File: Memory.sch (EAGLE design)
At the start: 4 parts, among them IC5 HM62256DIP

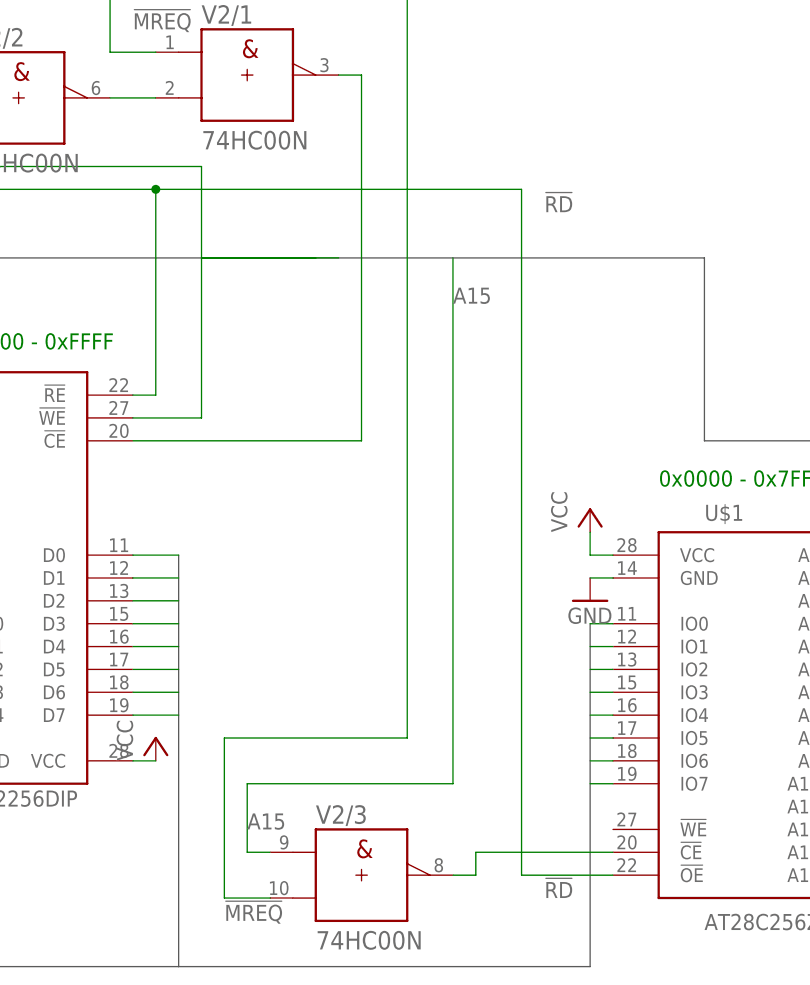
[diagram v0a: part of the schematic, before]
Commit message: Connect ROM WriteEnable so we can rewrite rom from the CPU
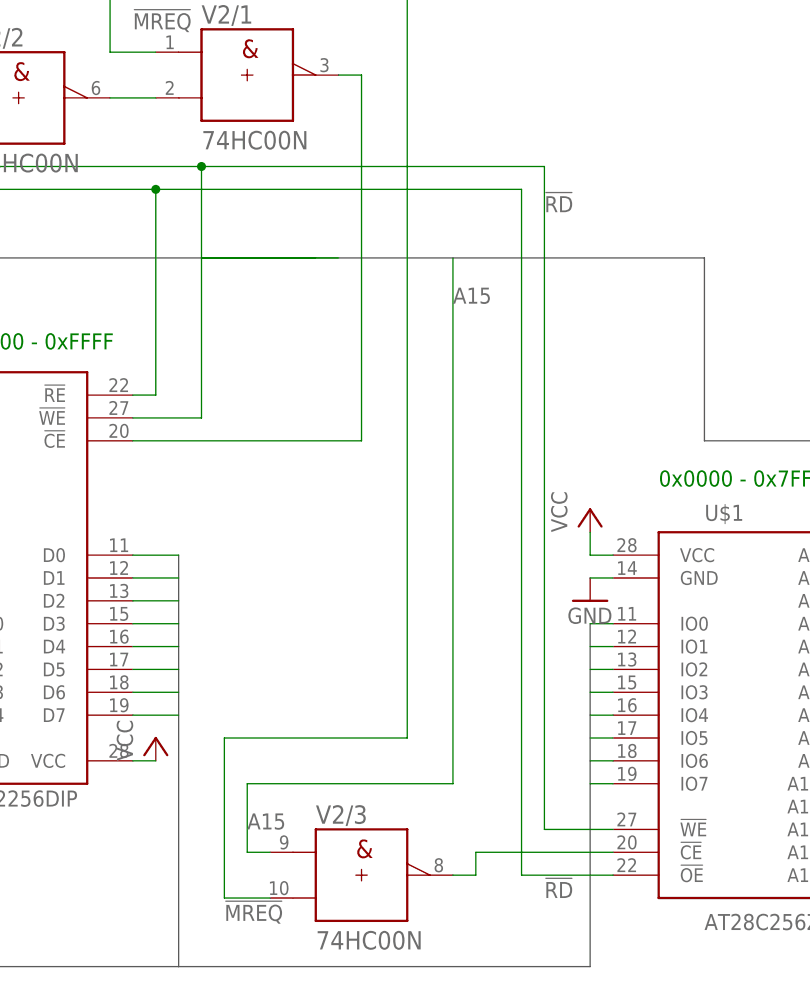
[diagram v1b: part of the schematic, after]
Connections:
- net !WR: now also U$1.!WE
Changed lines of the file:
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@@
 <wire x1="-66.04" y1="172.72" x2="-50.8" y2="172.72" width="0.1524" layer="91"/>
 <wire x1="-50.8" y1="172.72" x2="-50.8" y2="177.8" width="0.1524" layer="91"/>
+<wire x1="68.58" y1="177.8" x2="106.68" y2="177.8" width="0.1524" layer="91"/>
+<wire x1="106.68" y1="177.8" x2="106.68" y2="104.14" width="0.1524" layer="91"/>
+<junction x="68.58" y="177.8"/>
+<pinref part="U$1" gate="G$1" pin="!WE"/>
+<wire x1="106.68" y1="104.14" x2="114.3" y2="104.14" width="0.1524" layer="91"/>
 </segment>
 </net>

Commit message: Finish Modularization
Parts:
- renumbered IC5 to IC2, U$1 to IC1

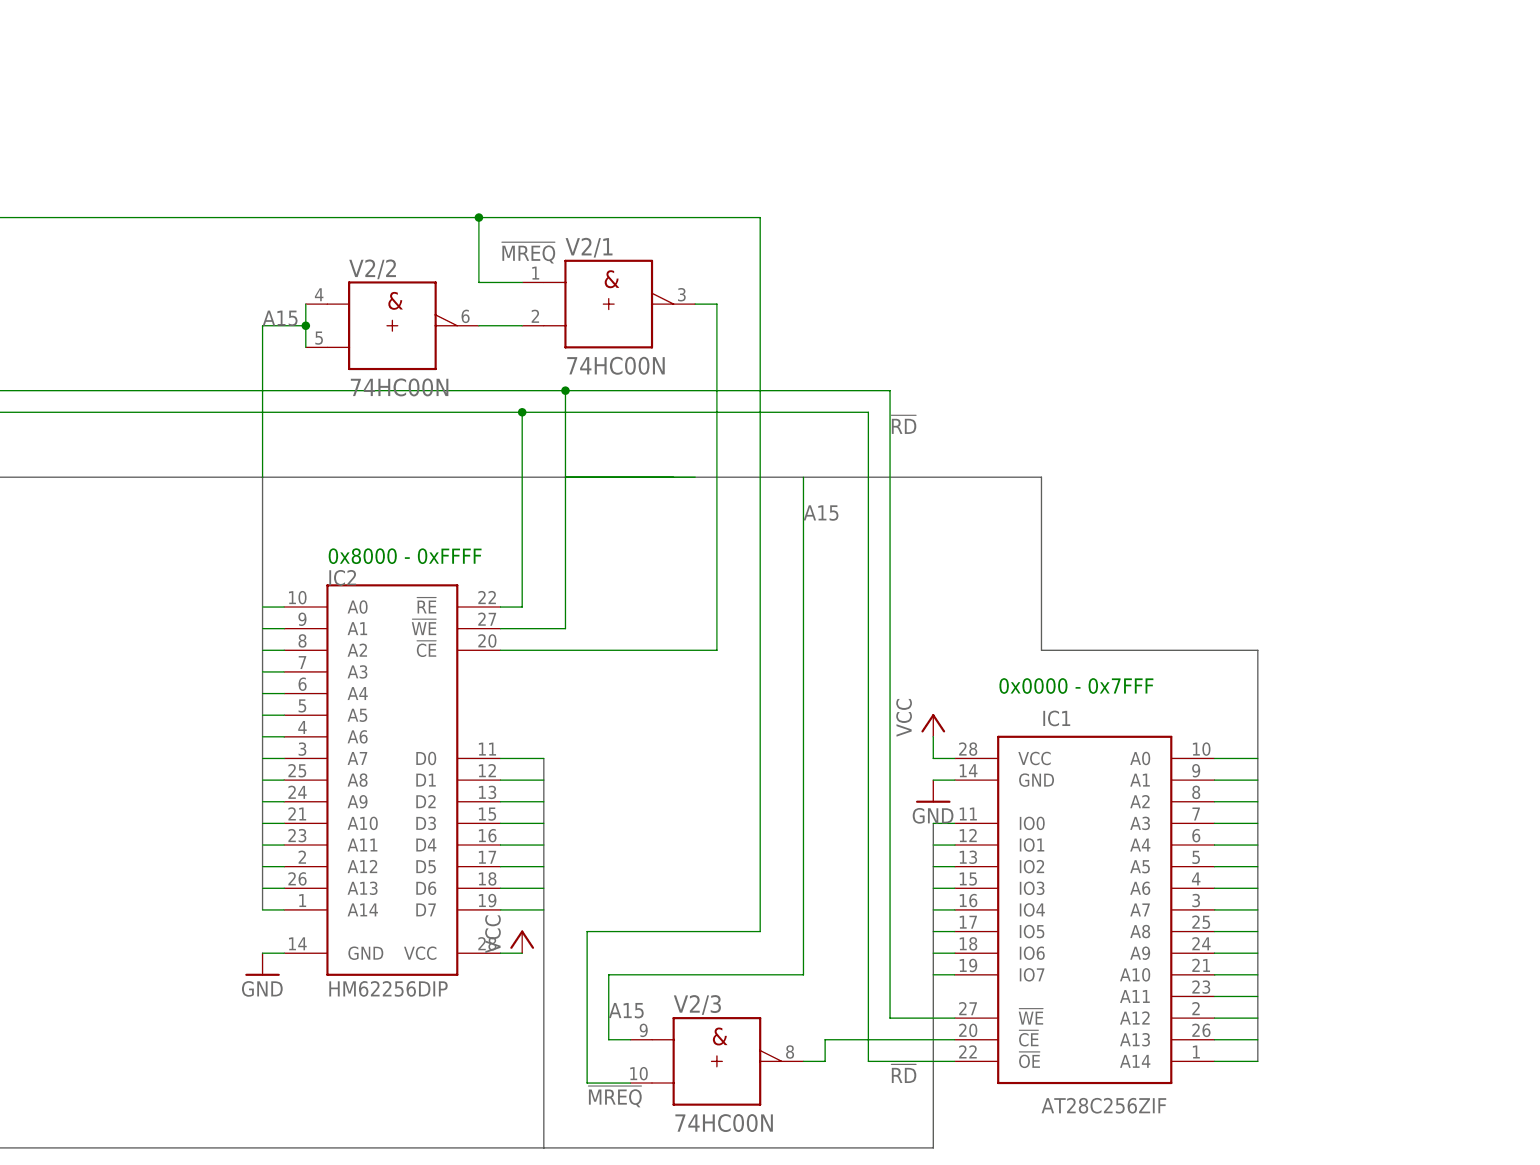
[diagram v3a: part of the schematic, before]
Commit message: Add Decoupling Capacitors.
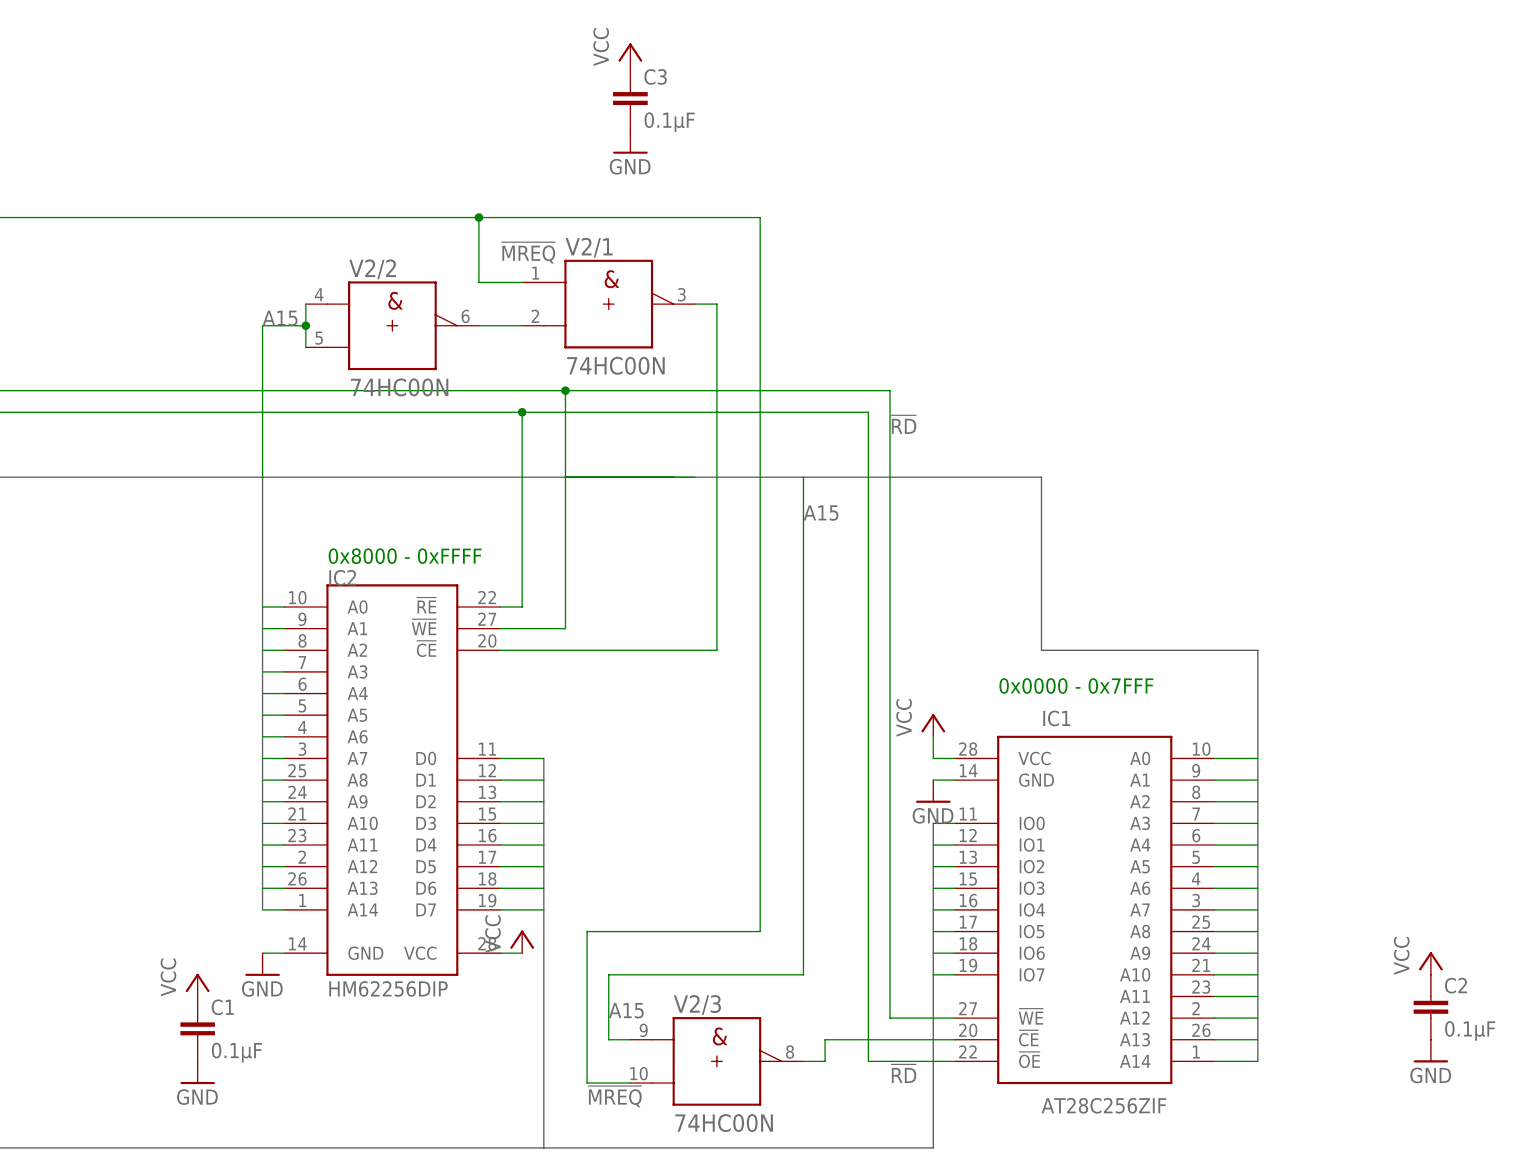
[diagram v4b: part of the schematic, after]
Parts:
- added C1, C2, C3: 0.1µF, capacitor-wima:C5/2.5
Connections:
- net GND: now also C1.2, C2.2, C3.2
- net VCC: now also C1.1, C2.1, C3.1
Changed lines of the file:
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@@
 <part name="GND4" library="supply1" deviceset="GND" device=""/>
 <part name="P+1" library="supply1" deviceset="VCC" device=""/>
+<part name="C1" library="capacitor-wima" deviceset="C" device="5/2.5" value="0.1µF"/>
+<part name="P+2" library="supply1" deviceset="VCC" device=""/>
+<part name="GND1" library="supply1" deviceset="GND" device=""/>
+<part name="C2" library="capacitor-wima" deviceset="C" device="5/2.5" value="0.1µF"/>
+<part name="P+4" library="supply1" deviceset="VCC" device=""/>
+<part name="GND2" library="supply1" deviceset="GND" device=""/>
+<part name="C3" library="capacitor-wima" deviceset="C" device="5/2.5" value="0.1µF"/>
+<part name="P+6" library="supply1" deviceset="VCC" device=""/>
+<part name="GND5" library="supply1" deviceset="GND" device=""/>
 </parts>
 <sheets>
@@
 <instance part="V2" gate="/+UB" x="-78.74" y="167.64"/>
 <instance part="V2" gate="/-UB" x="-86.36" y="167.64"/>
+<instance part="C1" gate="G$1" x="25.4" y="104.14"/>
+<instance part="P+2" gate="VCC" x="25.4" y="109.22"/>
+<instance part="GND1" gate="1" x="25.4" y="96.52"/>
+<instance part="C2" gate="G$1" x="170.18" y="106.68"/>
+<instance part="P+4" gate="VCC" x="170.18" y="111.76"/>
+<instance part="GND2" gate="1" x="170.18" y="99.06"/>
+<instance part="C3" gate="G$1" x="76.2" y="213.36"/>
+<instance part="P+6" gate="VCC" x="76.2" y="218.44"/>
+<instance part="GND5" gate="1" x="76.2" y="205.74"/>
 </instances>
 <busses>
@@
 <wire x1="-78.74" y1="170.18" x2="-78.74" y2="175.26" width="0.1524" layer="91"/>
 <junction x="-78.74" y="170.18"/>
+</segment>
+<segment>
+<pinref part="C1" gate="G$1" pin="1"/>
+<pinref part="P+2" gate="VCC" pin="VCC"/>
+</segment>
+<segment>
+<pinref part="C2" gate="G$1" pin="1"/>
+<pinref part="P+4" gate="VCC" pin="VCC"/>
+</segment>
+<segment>
+<pinref part="C3" gate="G$1" pin="1"/>
+<pinref part="P+6" gate="VCC" pin="VCC"/>
 </segment>
 </net>
@@
 <junction x="-86.36" y="165.1"/>
 </segment>
-</net>
+<segment>
+<pinref part="C1" gate="G$1" pin="2"/>
+<pinref part="GND1" gate="1" pin="GND"/>
+</segment>
+<segment>
+<pinref part="C2" gate="G$1" pin="2"/>
+<pinref part="GND2" gate="1" pin="GND"/>
+</segment>
+<segment>
+<pinref part="C3" gate="G$1" pin="2"/>
+<pinref part="GND5" gate="1" pin="GND"/>
+</segment>
+</net>

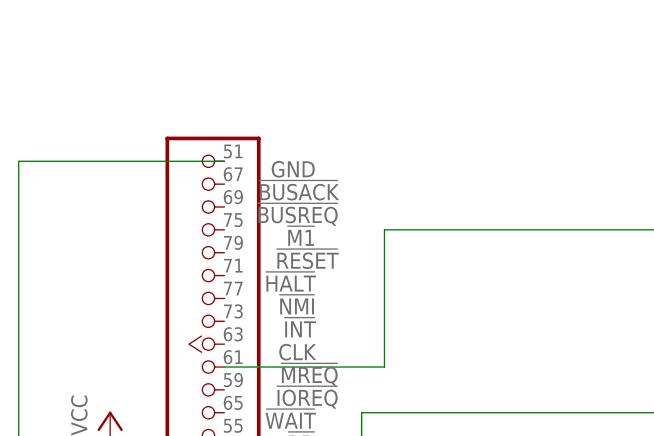
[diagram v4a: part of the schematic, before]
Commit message: Add Ground Rail to JEANNECTOR
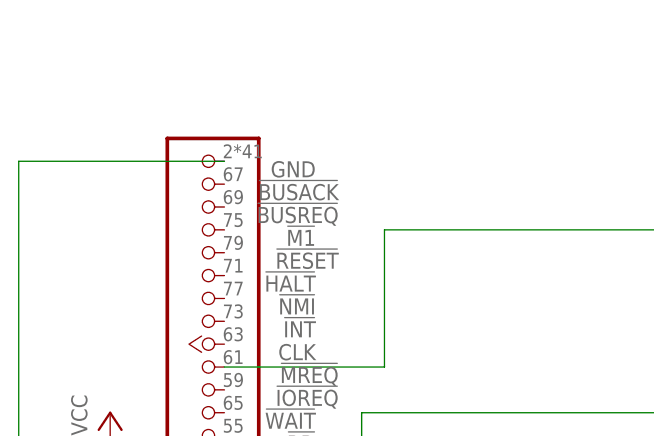
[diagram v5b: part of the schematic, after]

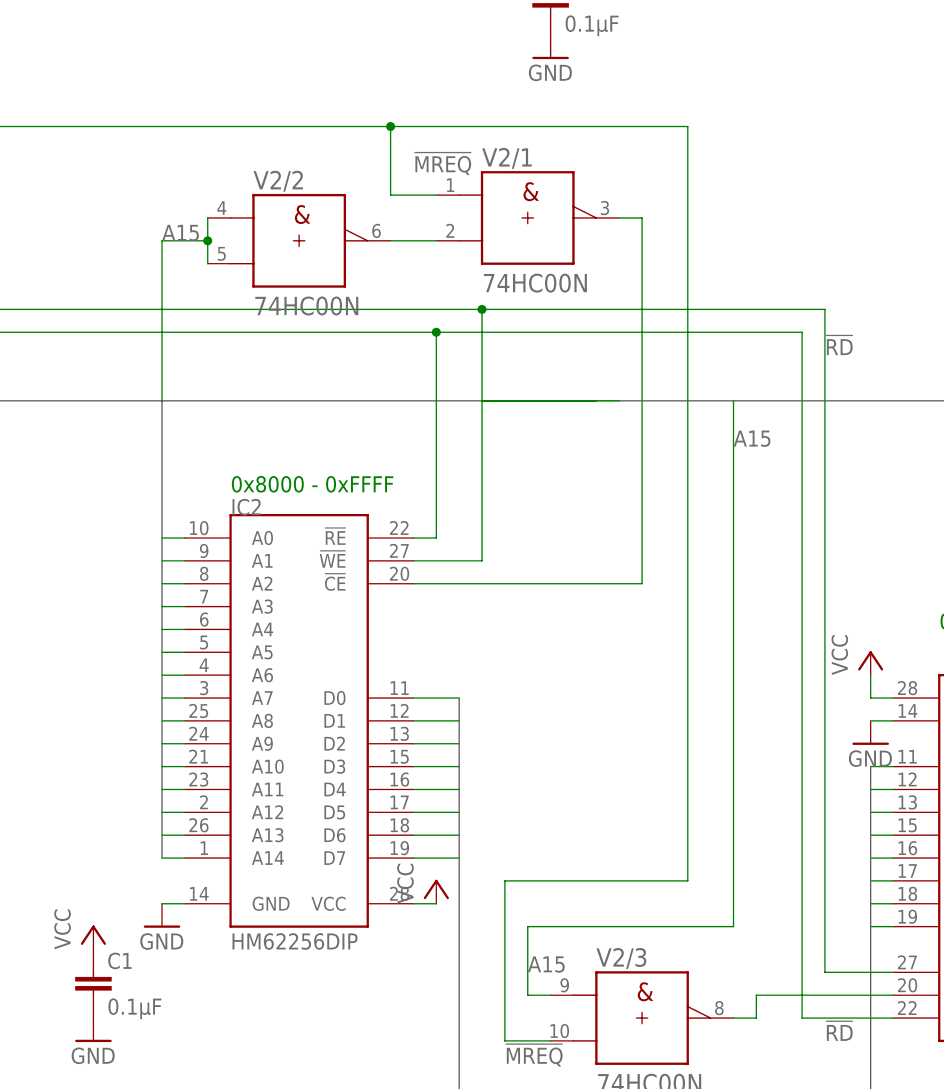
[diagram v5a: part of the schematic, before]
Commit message: Fix Memory Mapping inversely. Move Text on Muddi
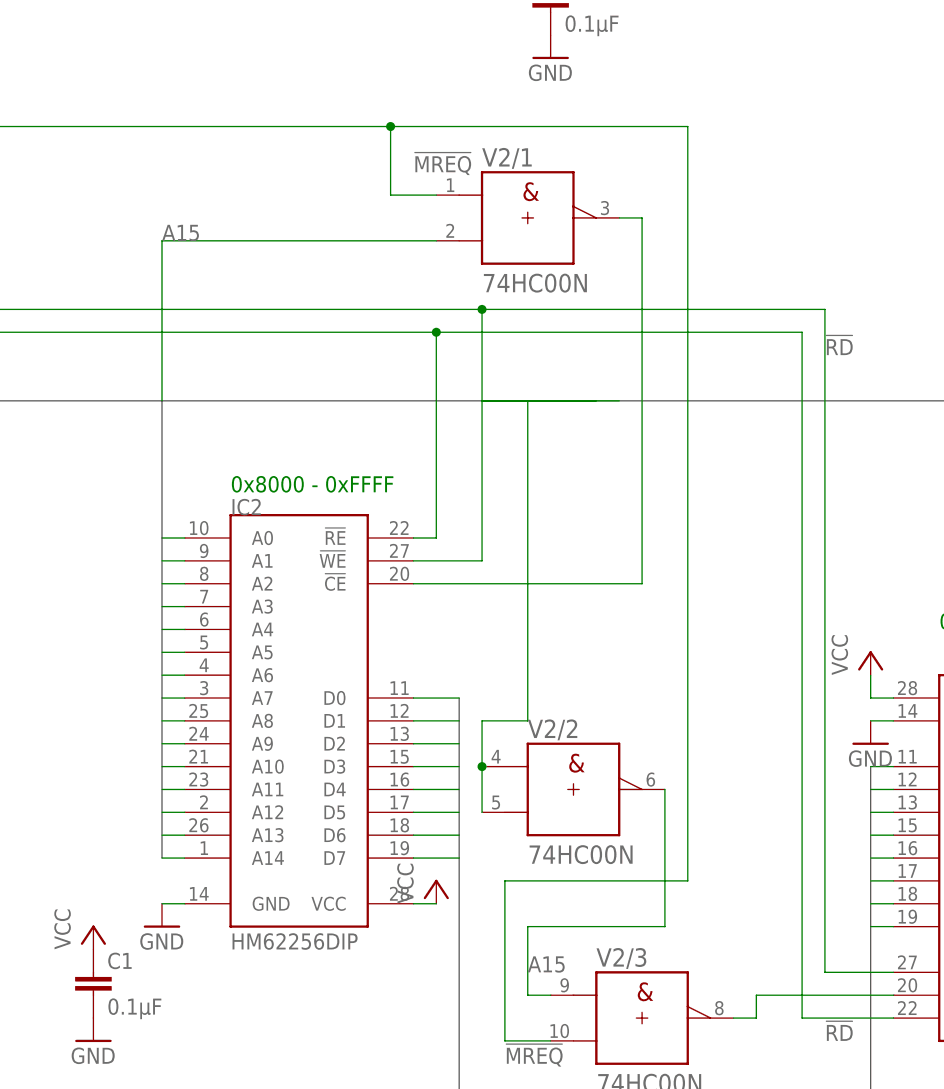
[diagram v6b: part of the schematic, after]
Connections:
- removed net N$4: V2/1.B, V2/2.Y
- net A15: now also V2/1.B, V2/2.Y
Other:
- moved on the sheet: V2/2
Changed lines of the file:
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@@
 <instance part="IC1" gate="G$1" x="129.54" y="114.3"/>
 <instance part="JP1" gate="A" x="-68.58" y="137.16" rot="R180"/>
-<instance part="V2" gate="/2" x="48.26" y="185.42"/>
+<instance part="V2" gate="/2" x="78.74" y="124.46"/>
 <instance part="V2" gate="/3" x="86.36" y="99.06"/>
 <instance part="GND4" gate="1" x="-83.82" y="162.56"/>
@@
 <segment>
 <wire x1="33.02" y1="167.64" x2="33.02" y2="185.42" width="0.1524" layer="91"/>
-<wire x1="33.02" y1="185.42" x2="38.1" y2="185.42" width="0.1524" layer="91"/>
-<wire x1="38.1" y1="185.42" x2="38.1" y2="182.88" width="0.1524" layer="91"/>
-<wire x1="38.1" y1="185.42" x2="38.1" y2="187.96" width="0.1524" layer="91"/>
-<junction x="38.1" y="185.42"/>
 <label x="33.02" y="185.42" size="1.778" layer="95"/>
-<pinref part="V2" gate="/2" pin="A"/>
-<pinref part="V2" gate="/2" pin="B"/>
+<pinref part="V2" gate="/1" pin="B"/>
+<wire x1="33.02" y1="185.42" x2="63.5" y2="185.42" width="0.1524" layer="91"/>
 </segment>
 <segment>
 <wire x1="73.66" y1="109.22" x2="73.66" y2="101.6" width="0.1524" layer="91"/>
 <wire x1="73.66" y1="101.6" x2="76.2" y2="101.6" width="0.1524" layer="91"/>
-<wire x1="96.52" y1="109.22" x2="73.66" y2="109.22" width="0.1524" layer="91"/>
-<wire x1="96.52" y1="109.22" x2="96.52" y2="167.64" width="0.1524" layer="91"/>
-<label x="96.52" y="162.56" size="1.778" layer="95"/>
+<wire x1="88.9" y1="109.22" x2="73.66" y2="109.22" width="0.1524" layer="91"/>
 <label x="73.66" y="104.14" size="1.778" layer="95"/>
 <pinref part="V2" gate="/3" pin="A"/>
+<pinref part="V2" gate="/2" pin="Y"/>
+<wire x1="88.9" y1="124.46" x2="88.9" y2="109.22" width="0.1524" layer="91"/>
 </segment>
 <segment>
 <pinref part="JP1" gate="A" pin="A15"/>
 <wire x1="-66.04" y1="165.1" x2="-38.1" y2="165.1" width="0.1524" layer="91"/>
+</segment>
+<segment>
+<wire x1="76.2" y1="167.64" x2="73.66" y2="167.64" width="0.1524" layer="91"/>
+<wire x1="73.66" y1="167.64" x2="73.66" y2="132.08" width="0.1524" layer="91"/>
+<wire x1="73.66" y1="132.08" x2="68.58" y2="132.08" width="0.1524" layer="91"/>
+<pinref part="V2" gate="/2" pin="A"/>
+<wire x1="68.58" y1="132.08" x2="68.58" y2="127" width="0.1524" layer="91"/>
+<pinref part="V2" gate="/2" pin="B"/>
+<wire x1="68.58" y1="127" x2="68.58" y2="121.92" width="0.1524" layer="91"/>
+<junction x="68.58" y="127"/>
 </segment>
 </net>
@@
 </segment>
 </net>
-<net name="N$4" class="0">
-<segment>
-<pinref part="V2" gate="/1" pin="B"/>
-<wire x1="58.42" y1="185.42" x2="63.5" y2="185.42" width="0.1524" layer="91"/>
-<pinref part="V2" gate="/2" pin="Y"/>
-</segment>
-</net>
